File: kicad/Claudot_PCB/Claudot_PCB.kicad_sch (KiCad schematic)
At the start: 52 parts, among them J1 Conn_01x04, SW1 SW_Push, SW10 SW_Push, SW11 SW_Push, SW12 RotaryEncoder, SW2 SW_Push, SW3 SW_Push, SW4 SW_Push, SW5 SW_Push, SW6 SW_Push, SW7 SW_Push, SW8 SW_Push, SW9 SW_Push, U1 RP2040, U2 W25Q16JVUXIQ, U3 AP2112K-3.3, Y1 12MHz

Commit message: Update schematic and pcb
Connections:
- net GND: now also SW_B1.3, SW_B1.4, SW_R1.3, SW_R1.4; no longer SW_B1.1, SW_R1.1
- net QSPI_SS: now also R4.2; no longer R4.1
- net ~{RESET}: now also SW_R1.1, SW_R1.2; no longer SW_R1.3
- new net: R4.1, SW_B1.1, SW_B1.2
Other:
- moved on the sheet: R3, R4, SW_B1
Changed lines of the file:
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@@
 	)
 	(junction
-		(at 48.26 189.23)
+		(at 34.29 189.23)
 		(diameter 0)
 		(color 0 0 0 0)
@@
 	(wire
 		(pts
-			(xy 45.72 189.23) (xy 48.26 189.23)
+			(xy 36.83 189.23) (xy 34.29 189.23)
 		)
 		(stroke
@@
 	(wire
 		(pts
-			(xy 48.26 189.23) (xy 50.8 189.23)
+			(xy 34.29 189.23) (xy 31.75 189.23)
 		)
 		(stroke
@@
 	(wire
 		(pts
-			(xy 48.26 186.69) (xy 48.26 189.23)
+			(xy 34.29 186.69) (xy 34.29 189.23)
 		)
 		(stroke
@@
 	(global_label "~{RESET}"
 		(shape input)
-		(at 40.64 173.99 0)
+		(at 30.48 173.99 180)
 		(fields_autoplaced yes)
 		(effects
@@
 				(size 1.27 1.27)
 			)
-			(justify left)
+			(justify right)
 		)
 		(property "Intersheetrefs" "${INTERSHEET_REFS}"
-			(at 49.3703 173.99 0)
+			(at 21.7497 173.99 0)
 			(effects
 				(font
 					(size 1.27 1.27)
 				)
-				(justify left)
+				(justify right)
 				(hide yes)
 			)
@@
 	(global_label "QSPI_SS"
 		(shape input)
-		(at 50.8 189.23 0)
+		(at 31.75 189.23 180)
 		(fields_autoplaced yes)
 		(effects
@@
 				(size 1.27 1.27)
 			)
-			(justify left)
+			(justify right)
 		)
 		(property "Intersheetrefs" "${INTERSHEET_REFS}"
-			(at 61.5866 189.23 0)
+			(at 20.9634 189.23 0)
 			(effects
 				(font
 					(size 1.27 1.27)
 				)
-				(justify left)
+				(justify right)
 				(hide yes)
 			)
@@
 	(symbol
 		(lib_id "power:+3V3")
-		(at 48.26 181.61 0)
+		(at 34.29 181.61 0)
+		(mirror y)
 		(unit 1)
 		(exclude_from_sim no)
@@
 		(dnp no)
 		(property "Reference" "#PWR024"
-			(at 48.26 185.42 0)
+			(at 34.29 185.42 0)
 			(effects
 				(font
@@
 		)
 		(property "Value" "+3V3"
-			(at 48.26 177.8 0)
+			(at 34.29 177.8 0)
 			(effects
 				(font
@@
 		)
 		(property "Footprint" ""
-			(at 48.26 181.61 0)
+			(at 34.29 181.61 0)
 			(effects
 				(font
@@
 		)
 		(property "Datasheet" ""
-			(at 48.26 181.61 0)
+			(at 34.29 181.61 0)
 			(effects
 				(font
@@
 		)
 		(property "Description" ""
-			(at 48.26 181.61 0)
+			(at 34.29 181.61 0)
 			(effects
 				(font
@@
 	(symbol
 		(lib_id "power:GND")
-		(at 30.48 189.23 0)
+		(at 52.07 189.23 0)
+		(mirror y)
 		(unit 1)
 		(exclude_from_sim no)
@@
 		(fields_autoplaced yes)
 		(property "Reference" "#PWR027"
-			(at 30.48 195.58 0)
+			(at 52.07 195.58 0)
 			(effects
 				(font
@@
 		)
 		(property "Value" "GND"
-			(at 30.48 194.31 0)
+			(at 52.07 194.31 0)
 			(effects
 				(font
@@
 		)
 		(property "Footprint" ""
-			(at 30.48 189.23 0)
+			(at 52.07 189.23 0)
 			(effects
 				(font
@@
 		)
 		(property "Datasheet" ""
-			(at 30.48 189.23 0)
+			(at 52.07 189.23 0)
 			(effects
 				(font
@@
 		)
 		(property "Description" ""
-			(at 30.48 189.23 0)
+			(at 52.07 189.23 0)
 			(effects
 				(font
@@
 		(on_board yes)
 		(dnp no)
-		(fields_autoplaced yes)
 		(property "Reference" "SW_R1"
 			(at 35.56 166.37 0)
@@
 		(pin "3"
 		)
+		(pin "2"
+		)
+		(pin "4"
+		)
 		(instances
 			(project ""
@@
 	(symbol
 		(lib_id "Device:R_Small")
-		(at 48.26 184.15 0)
+		(at 34.29 184.15 0)
+		(mirror y)
 		(unit 1)
 		(exclude_from_sim no)
@@
 		(dnp no)
 		(property "Reference" "R3"
-			(at 47.244 184.15 0)
+			(at 35.306 184.15 0)
 			(effects
 				(font
@@
 		)
 		(property "Value" "10K"
-			(at 50.165 184.15 90)
+			(at 32.385 184.15 90)
 			(effects
 				(font
@@
 		)
 		(property "Footprint" "Resistor_SMD:R_0402_1005Metric"
-			(at 48.26 184.15 0)
+			(at 34.29 184.15 0)
 			(effects
 				(font
@@
 		)
 		(property "Datasheet" "~"
-			(at 48.26 184.15 0)
+			(at 34.29 184.15 0)
 			(effects
 				(font
@@
 		)
 		(property "Description" ""
-			(at 48.26 184.15 0)
+			(at 34.29 184.15 0)
 			(effects
 				(font
@@
 		)
 		(property "LCSC" "C25744"
-			(at 48.26 184.15 0)
+			(at 34.29 184.15 0)
 			(effects
 				(font
@@
 	(symbol
 		(lib_id "power:GND")
-		(at 30.48 173.99 0)
+		(at 40.64 173.99 0)
+		(mirror y)
 		(unit 1)
 		(exclude_from_sim no)
@@
 		(fields_autoplaced yes)
 		(property "Reference" "#PWR026"
-			(at 30.48 180.34 0)
+			(at 40.64 180.34 0)
 			(effects
 				(font
@@
 		)
 		(property "Value" "GND"
-			(at 30.48 179.07 0)
+			(at 40.64 179.07 0)
 			(effects
 				(font
@@
 		)
 		(property "Footprint" ""
-			(at 30.48 173.99 0)
+			(at 40.64 173.99 0)
 			(effects
 				(font
@@
 		)
 		(property "Datasheet" ""
-			(at 30.48 173.99 0)
+			(at 40.64 173.99 0)
 			(effects
 				(font
@@
 		)
 		(property "Description" ""
-			(at 30.48 173.99 0)
+			(at 40.64 173.99 0)
 			(effects
 				(font
@@
 	(symbol
 		(lib_id "Device:R_Small")
-		(at 43.18 189.23 270)
+		(at 39.37 189.23 270)
 		(unit 1)
 		(exclude_from_sim no)
@@
 		(dnp no)
 		(property "Reference" "R4"
-			(at 43.18 187.325 90)
+			(at 39.37 187.325 90)
 			(effects
 				(font
@@
 		)
 		(property "Value" "1K"
-			(at 43.18 191.135 90)
+			(at 39.37 191.135 90)
 			(effects
 				(font
@@
 		)
 		(property "Footprint" "Resistor_SMD:R_0402_1005Metric"
-			(at 43.18 189.23 0)
+			(at 39.37 189.23 0)
 			(effects
 				(font
@@
 		)
 		(property "Datasheet" "~"
-			(at 43.18 189.23 0)
+			(at 39.37 189.23 0)
 			(effects
 				(font
@@
 		)
 		(property "Description" ""
-			(at 43.18 189.23 0)
+			(at 39.37 189.23 0)
 			(effects
 				(font
@@
 		)
 		(property "LCSC" "C11702"
-			(at 43.18 189.23 0)
+			(at 39.37 189.23 0)
 			(effects
 				(font
@@
 	(symbol
 		(lib_id "Library:SKRP_Switch")
-		(at 35.56 189.23 0)
+		(at 46.99 189.23 0)
 		(unit 1)
 		(exclude_from_sim no)
@@
 		(on_board yes)
 		(dnp no)
-		(fields_autoplaced yes)
 		(property "Reference" "SW_B1"
-			(at 35.56 181.61 0)
+			(at 46.99 181.61 0)
 			(effects
 				(font
@@
 		)
 		(property "Value" "SKRP_Switch"
-			(at 35.56 184.15 0)
+			(at 46.99 184.15 0)
 			(effects
 				(font
@@
 		)
 		(property "Footprint" "Library:SKRP_Switch"
-			(at 35.56 184.15 0)
+			(at 46.99 184.15 0)
 			(effects
 				(font
@@
 		)
 		(property "Datasheet" ""
-			(at 35.56 184.15 0)
+			(at 46.99 184.15 0)
 			(effects
 				(font
@@
 		)
 		(property "Description" ""
-			(at 35.56 189.23 0)
+			(at 46.99 189.23 0)
 			(effects
 				(font
@@
 		(pin "3"
 		)
+		(pin "2"
+		)
+		(pin "4"
+		)
 		(instances

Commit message: Update schematic and pcb
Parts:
- J1: value Conn_01x04 -> AFC01-S04FCC-00
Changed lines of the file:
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@@
 			)
 		)
-		(property "Value" "Conn_01x04"
+		(property "Value" "AFC01-S04FCC-00"
 			(at 34.29 76.1999 0)
 			(effects

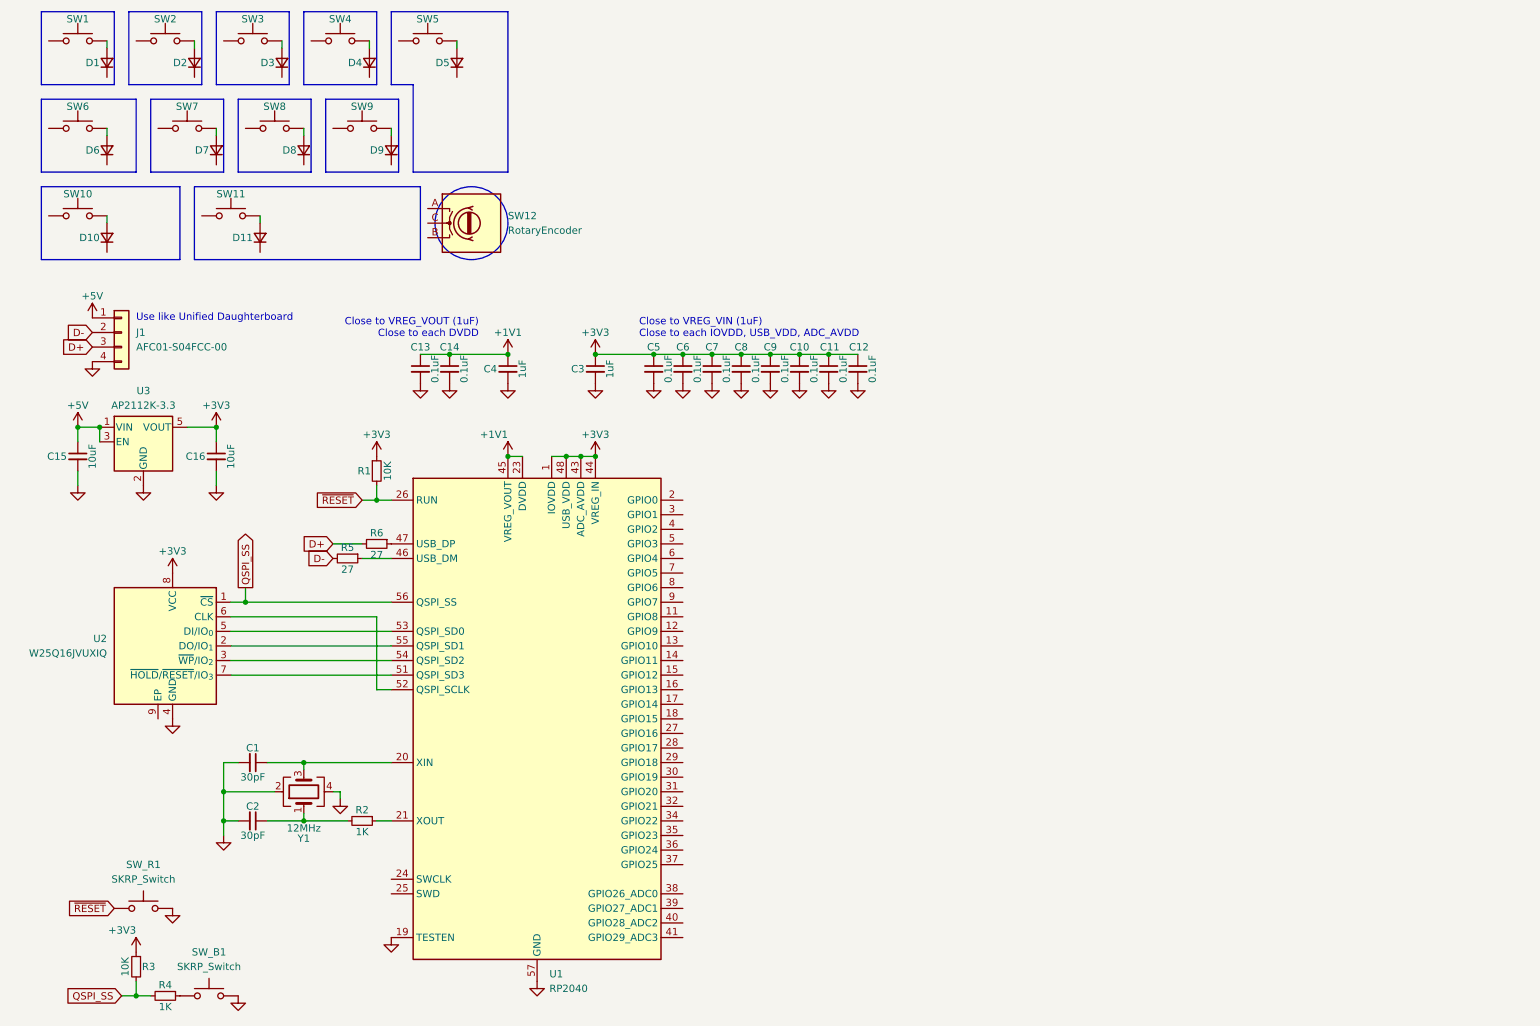
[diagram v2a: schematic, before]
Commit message: Add USB-C connector
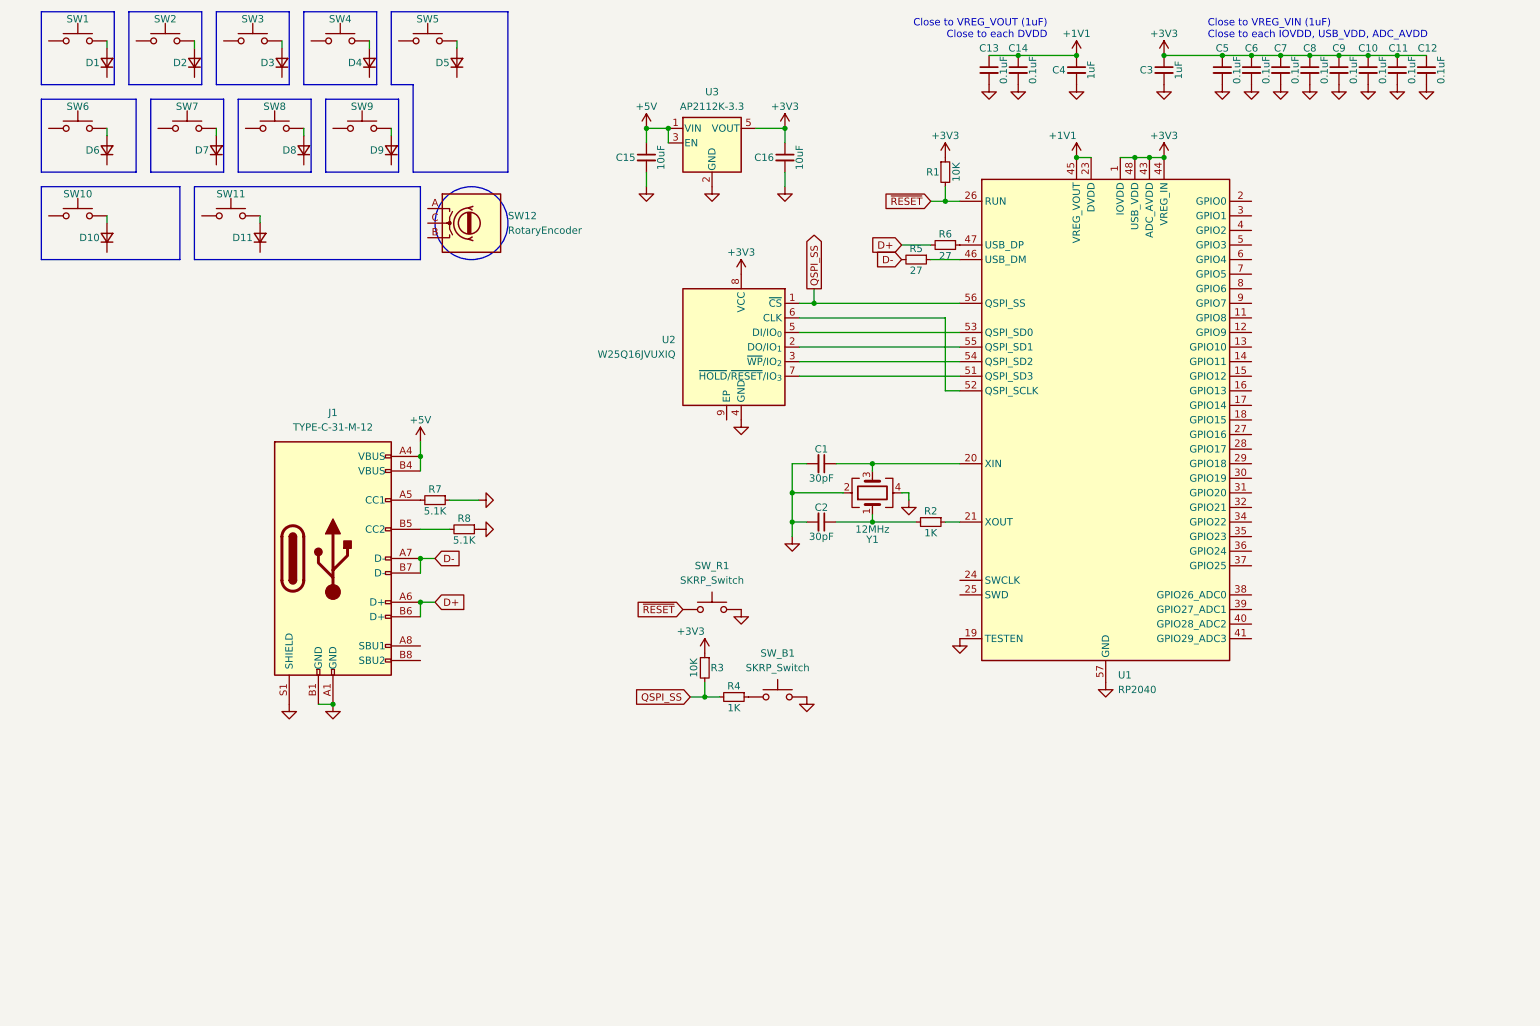
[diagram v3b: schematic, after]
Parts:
- removed J1: AFC01-S04FCC-00, Library:AFC01-S04FCC-00, symbol Connector_Generic:Conn_01x04
- added J1: TYPE-C-31-M-12, Library:TYPE-C-31-M-12, symbol Library:TYPE-C-31-M-12
- added R7, R8: 5.1K, Library:R_0402, symbol Device:R_Small
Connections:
- net +5V: now also J1.A4 (VBUS), J1.B4 (VBUS)
- net D+: now also J1.A6 (D+), J1.B6 (D+)
- net D-: now also J1.A7 (D-), J1.B7 (D-)
- net GND: now also J1.A1 (GND), J1.B1 (GND), J1.S1 (SHIELD), R7.1, R8.1
- new net: J1.A5 (CC1), R7.2
- new net: J1.B5 (CC2), R8.2
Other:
- note removed: "Use like Unified Daughterboard"
- moved on the sheet: C1, C10, C11, C12, C13, C14, C15, C16, C2, C3, C4, C5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

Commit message: Update schematic and pcb
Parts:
- added F1: ASMD1206-150, Fuse:Fuse_1206_3216Metric, symbol Device:Polyfuse
- added TVS-D1: SMF6V0A, Diode_SMD:D_SMF, symbol Diode:SMF6V0A
- J1: LCSC (none) -> C165948
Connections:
- net +5V: now also F1.2, TVS-D1.1 (A1); no longer J1.A4 (VBUS), J1.B4 (VBUS)
- net GND: now also J1.S (SHIELD), TVS-D1.2 (A2); no longer J1.S1 (SHIELD)
- new net VBUS: F1.1, J1.A4 (VBUS), J1.B4 (VBUS)

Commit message: Update schematic and pcb
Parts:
- added CA1, CB1: 0.1uF, Library:C_0402, symbol Device:C_Small
- added RA1, RA2, RB1, RB2: 10K, Library:R_0402, symbol Device:R_Small
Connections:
- net +3V3: now also RA1.1, RB1.1
- net GND: now also SW12.C, CA1.2, CB1.2
- net SW12-A: now reaches SW12.A
- net SW12-A: now also RA1.2, RA2.1
- net SW12-B: now reaches SW12.B
- net SW12-B: now also RB1.2, RB2.1
- new net IN-A: CA1.1, RA2.2
- new net IN-B: CB1.1, RB2.2
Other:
- moved on the sheet: C1, C10, C11, C12, C13, C14, C15, C16, C2, C3, C4, C5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

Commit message: Update schematic and pcb
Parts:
- F1: footprint Fuse:Fuse_1206_3216Metric -> Library:F_1206
- TVS-D1: footprint Diode_SMD:D_SMF -> Library:SMF6.0A; LCSC (none) -> C178260
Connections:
- net GND: now also R7.2, R8.2; no longer R7.1, R8.1
- net at J1.A5 (CC1): now also R7.1; no longer R7.2
- net at J1.B5 (CC2): now also R8.1; no longer R8.2
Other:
- moved on the sheet: R7, R8
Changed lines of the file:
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@@
 			)
 		)
-		(property "Footprint" "Diode_SMD:D_SMF"
+		(property "Footprint" "Library:SMF6.0A"
 			(at 106.68 143.51 0)
 			(effects
@@
 			)
 		)
-		(property "Datasheet" "https://www.vishay.com/doc?85881"
+		(property "Datasheet" "~"
 			(at 111.76 142.24 0)
 			(effects
@@
 			)
 		)
-		(property "Description" "200W unidirectional Transil Transient Voltage Suppressor, 6Vrwm, SMF"
+		(property "Description" ""
 			(at 111.76 143.51 0)
 			(effects
@@
 			)
 		)
+		(property "LCSC" "C178260"
+			(at 111.76 143.51 90)
+			(effects
+				(font
+					(size 1.27 1.27)
+				)
+				(hide yes)
+			)
+		)
 		(pin "1"
 		)
@@
 	(symbol
 		(lib_id "Device:R_Small")
-		(at 86.36 147.32 270)
+		(at 86.36 147.32 90)
 		(unit 1)
 		(exclude_from_sim no)
@@
 		(dnp no)
 		(property "Reference" "R7"
-			(at 86.36 145.415 90)
+			(at 86.36 149.225 90)
 			(effects
 				(font
@@
 		)
 		(property "Value" "5.1K"
-			(at 86.36 149.225 90)
+			(at 86.36 145.415 90)
 			(effects
 				(font
@@
 			)
 		)
-		(property "Footprint" "Fuse:Fuse_1206_3216Metric"
+		(property "Footprint" "Library:F_1206"
 			(at 110.49 138.43 0)
 			(effects
@@
 	(symbol
 		(lib_id "Device:R_Small")
-		(at 91.44 152.4 270)
+		(at 91.44 152.4 90)
 		(unit 1)
 		(exclude_from_sim no)
@@
 		(dnp no)
 		(property "Reference" "R8"
-			(at 91.44 150.495 90)
+			(at 91.44 154.305 90)
 			(effects
 				(font
@@
 		)
 		(property "Value" "5.1K"
-			(at 91.44 154.305 90)
+			(at 91.44 150.495 90)
 			(effects
 				(font

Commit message: Update schematic and pcb
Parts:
- R3, R4: footprint Resistor_SMD:R_0402_1005Metric -> Library:R_0402
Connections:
- net QSPI_SS: now also R4.1; no longer R4.2
- net at SW_B1.1, SW_B1.2: now also R4.2; no longer R4.1
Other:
- moved on the sheet: R4
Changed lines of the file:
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@@
 			)
 		)
-		(property "Footprint" "Resistor_SMD:R_0402_1005Metric"
+		(property "Footprint" "Library:R_0402"
 			(at 140.97 139.7 0)
 			(effects
@@
 	(symbol
 		(lib_id "Device:R_Small")
-		(at 146.05 144.78 270)
+		(at 146.05 144.78 90)
 		(unit 1)
 		(exclude_from_sim no)
@@
 		(dnp no)
 		(property "Reference" "R4"
-			(at 146.05 142.875 90)
+			(at 146.05 146.685 90)
 			(effects
 				(font
@@
 		)
 		(property "Value" "1K"
-			(at 146.05 146.685 90)
+			(at 146.05 142.875 90)
 			(effects
 				(font
@@
 			)
 		)
-		(property "Footprint" "Resistor_SMD:R_0402_1005Metric"
+		(property "Footprint" "Library:R_0402"
 			(at 146.05 144.78 0)
 			(effects

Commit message: Update schematic and pcb
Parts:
- added J2: Conn_01x12, Library:AFC01-S12FCC-00, symbol Connector_Generic:Conn_01x12
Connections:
- net at U1.29 (GPIO18): now also J2.1 (Pin_1)
- net at U1.30 (GPIO19): now also J2.2 (Pin_2)
- net at U1.31 (GPIO20): now also J2.3 (Pin_3)
- net at U1.32 (GPIO21): now also J2.4 (Pin_4)
- net at U1.34 (GPIO22): now also J2.5 (Pin_5)
- net at U1.35 (GPIO23): now also J2.6 (Pin_6)
- net at U1.36 (GPIO24): now also J2.7 (Pin_7)
- net at U1.37 (GPIO25): now also J2.8 (Pin_8)
- net at U1.38 (GPIO26_ADC0): now also J2.9 (Pin_9)
- net at U1.39 (GPIO27_ADC1): now also J2.10 (Pin_10)
- net at U1.40 (GPIO28_ADC2): now also J2.11 (Pin_11)
- net at U1.41 (GPIO29_ADC3): now also J2.12 (Pin_12)
